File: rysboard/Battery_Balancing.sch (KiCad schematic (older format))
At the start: 50 parts, among them J4 Cell3, J5 Cell2, J6 Cell1, J7 Power_SW

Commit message: NST847BDP6T5G Added, more conections done
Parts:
- removed Q? (x3): PLACEHOLDER, Package_TO_SOT_THT:TO-92_Inline, symbol Transistor_FET:2N7000
- added Q1, Q2: DMP3036SSD-13, Package_SO:SO-8_5.3x6.2mm_P1.27mm, symbol rysboard:DMP3036SSD-13
- U10, U7, U8: renamed from U?; footprint (none) -> Package_SO:SO-8_5.3x6.2mm_P1.27mm
- gave numbers to parts that had none: 40
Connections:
- net PACK-: now also Q1.5 (d), Q1.6 (d)
- net V_BAT_AF_PROT-: now also Q2.1 (S1), Q2.3 (S2)
- net at D12.2 (A2), J6.1 (Pin_1): now also Q2.5 (d), Q2.6 (d), Q2.7 (d), Q2.8 (d)
- net at R15.1: now also Q2.2 (G1), Q2.4 (G2)
- net at R25.1, R30.1, R32.1: now also Q1.7 (d), Q1.8 (d)
- net at D16.1 (K), R33.2, R34.1: now also Q1.4 (G2)
- net at R31.1, R32.2: now also Q1.2 (G1)
- new net: Q1.1 (S1), Q1.3 (S2)
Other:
- moved on the sheet: R15

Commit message: new mosfet footprints
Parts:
- D10, D11, D12: footprint (none) -> Diode_SMD:D_SOD-128
- R15, R16, R17, R18, R19, R20, R21, R22, R23, R24, R30, R37, R38: footprint (none) -> Resistor_SMD:R_0603_1608Metric
- U11: footprint (none) -> Package_SO:TSSOP-24_4.4x7.8mm_P0.65mm
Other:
- note removed: "for lower resistance 2 mosfets on parrarel\n"
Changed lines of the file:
@@
 F 0 "R15" V 1643 3300 50  0000 C CNN
 F 1 "10KR" V 1734 3300 50  0000 C CNN
-F 2 "" V 1780 3300 50  0001 C CNN
+F 2 "Resistor_SMD:R_0603_1608Metric" V 1780 3300 50  0001 C CNN
 F 3 "~" H 1850 3300 50  0001 C CNN
 	1    1850 3300
@@
 F 0 "D10" V 1554 1730 50  0000 L CNN
 F 1 "D_TVS" V 1645 1730 50  0000 L CNN
-F 2 "" H 1600 1650 50  0001 C CNN
+F 2 "Diode_SMD:D_SOD-128" H 1600 1650 50  0001 C CNN
 F 3 "~" H 1600 1650 50  0001 C CNN
 	1    1600 1650
@@
 F 0 "D11" V 1554 2580 50  0000 L CNN
 F 1 "D_TVS" V 1645 2580 50  0000 L CNN
-F 2 "" H 1600 2500 50  0001 C CNN
+F 2 "Diode_SMD:D_SOD-128" H 1600 2500 50  0001 C CNN
 F 3 "~" H 1600 2500 50  0001 C CNN
 	1    1600 2500
@@
 F 0 "D12" V 1554 3380 50  0000 L CNN
 F 1 "D_TVS" V 1645 3380 50  0000 L CNN
-F 2 "" H 1600 3300 50  0001 C CNN
+F 2 "Diode_SMD:D_SOD-128" H 1600 3300 50  0001 C CNN
 F 3 "~" H 1600 3300 50  0001 C CNN
 	1    1600 3300
@@
 	1600 1400 2400 1400
 Connection ~ 1600 1500
-Text Notes 2550 750  0    50   ~ 0
-for lower resistance 2 mosfets on parrarel\n
 Wire Wire Line
 	4350 1350 4750 1350
@@
 F 0 "R24" V 2793 3450 50  0000 C CNN
 F 1 "10KR" V 2884 3450 50  0000 C CNN
-F 2 "" V 2930 3450 50  0001 C CNN
+F 2 "Resistor_SMD:R_0603_1608Metric" V 2930 3450 50  0001 C CNN
 F 3 "~" H 3000 3450 50  0001 C CNN
 	1    3000 3450
@@
 F 0 "R23" V 2793 2300 50  0000 C CNN
 F 1 "10KR" V 2884 2300 50  0000 C CNN
-F 2 "" V 2930 2300 50  0001 C CNN
+F 2 "Resistor_SMD:R_0603_1608Metric" V 2930 2300 50  0001 C CNN
 F 3 "~" H 3000 2300 50  0001 C CNN
 	1    3000 2300
@@
 F 0 "R22" V 2793 1700 50  0000 C CNN
 F 1 "10KR" V 2884 1700 50  0000 C CNN
-F 2 "" V 2930 1700 50  0001 C CNN
+F 2 "Resistor_SMD:R_0603_1608Metric" V 2930 1700 50  0001 C CNN
 F 3 "~" H 3000 1700 50  0001 C CNN
 	1    3000 1700
@@
 F 0 "U11" H 4050 6915 50  0000 C CNN
 F 1 "bq77915" H 4050 6824 50  0000 C CNN
-F 2 "" H 4150 5650 50  0001 C CNN
+F 2 "Package_SO:TSSOP-24_4.4x7.8mm_P0.65mm" H 4150 5650 50  0001 C CNN
 F 3 "" H 4150 5650 50  0001 C CNN
 	1    4050 5750
@@
 F 0 "R38" H 5180 7154 50  0000 R CNN
 F 1 "470KR5%" H 5180 7245 50  0000 R CNN
-F 2 "" V 5180 7200 50  0001 C CNN
+F 2 "Resistor_SMD:R_0603_1608Metric" V 5180 7200 50  0001 C CNN
 F 3 "~" H 5250 7200 50  0001 C CNN
 	1    5250 7200
@@
 F 0 "R17" V 1793 5500 50  0000 C CNN
 F 1 "33R5%" V 1884 5500 50  0000 C CNN
-F 2 "" V 1930 5500 50  0001 C CNN
+F 2 "Resistor_SMD:R_0603_1608Metric" V 1930 5500 50  0001 C CNN
 F 3 "~" H 2000 5500 50  0001 C CNN
 	1    2000 5500
@@
 F 0 "R16" V 1793 4700 50  0000 C CNN
 F 1 "1KR1%" V 1884 4700 50  0000 C CNN
-F 2 "" V 1930 4700 50  0001 C CNN
+F 2 "Resistor_SMD:R_0603_1608Metric" V 1930 4700 50  0001 C CNN
 F 3 "~" H 2000 4700 50  0001 C CNN
 	1    2000 4700
@@
 F 0 "R37" V 4900 6100 50  0000 C CNN
 F 1 "470KR1%" V 5000 6100 50  0000 C CNN
-F 2 "" V 5030 6100 50  0001 C CNN
+F 2 "Resistor_SMD:R_0603_1608Metric" V 5030 6100 50  0001 C CNN
 F 3 "~" H 5100 6100 50  0001 C CNN
 	1    5100 6100
@@
 F 0 "R21" H 2850 6900 50  0000 R CNN
 F 1 "100R" H 3000 7150 50  0000 R CNN
-F 2 "" V 2830 6950 50  0001 C CNN
+F 2 "Resistor_SMD:R_0603_1608Metric" V 2830 6950 50  0001 C CNN
 F 3 "~" H 2900 6950 50  0001 C CNN
 	1    2900 6950
@@
 F 0 "R30" H 3350 6900 50  0000 R CNN
 F 1 "100R" H 3300 7100 50  0000 R CNN
-F 2 "" V 3130 6950 50  0001 C CNN
+F 2 "Resistor_SMD:R_0603_1608Metric" V 3130 6950 50  0001 C CNN
 F 3 "~" H 3200 6950 50  0001 C CNN
 	1    3200 6950
@@
 F 0 "R18" V 1793 6000 50  0000 C CNN
 F 1 "33R5%" V 1884 6000 50  0000 C CNN
-F 2 "" V 1930 6000 50  0001 C CNN
+F 2 "Resistor_SMD:R_0603_1608Metric" V 1930 6000 50  0001 C CNN
 F 3 "~" H 2000 6000 50  0001 C CNN
 	1    2000 6000
@@
 F 0 "R19" V 1793 6500 50  0000 C CNN
 F 1 "33R5%" V 1884 6500 50  0000 C CNN
-F 2 "" V 1930 6500 50  0001 C CNN
+F 2 "Resistor_SMD:R_0603_1608Metric" V 1930 6500 50  0001 C CNN
 F 3 "~" H 2000 6500 50  0001 C CNN
 	1    2000 6500
@@
 F 0 "R20" V 1793 7100 50  0000 C CNN
 F 1 "33R5%" V 1884 7100 50  0000 C CNN
-F 2 "" V 1930 7100 50  0001 C CNN
+F 2 "Resistor_SMD:R_0603_1608Metric" V 1930 7100 50  0001 C CNN
 F 3 "~" H 2000 7100 50  0001 C CNN
 	1    2000 7100

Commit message: Fixed library, added a few MOSFET layouts
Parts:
- removed D14, D15: D_Zener, symbol Device:D_Zener
- removed Q2: DMP3036SSD-13, Package_SO:SO-8_5.3x6.2mm_P1.27mm, symbol rysboard:DMP3036SSD-13
- removed U10, U7, U8: DMP3036SSD, Package_SO:SO-8_5.3x6.2mm_P1.27mm, symbol rysboard:DMP3036SSD
- added Q13: SI7997DP-T1-GE3, Package_SO:PowerPAK_SO-8_Dual, symbol rysboard:SI7997DP-T1-GE3
- added Q14: DMP2075UFDB-7-alt, SamacSys_Parts:DMP2075UFDB7, symbol SamacSys_Parts:DMP2075UFDB-7-alt
- added Q?: Si7938DP-T1-GE3, Package_SO:PowerPAK_SO-8_Dual, symbol rysboard:Si7938DP-T1-GE3
- Q1: footprint Package_SO:SO-8_5.3x6.2mm_P1.27mm -> Package_SO:SO-8_3.9x4.9mm_P1.27mm
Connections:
- net V_BAT_AF_PROT-: now also Q?.1 (S1)
- net V_CELL_1: now also Q14.1 (S1)
- net V_CELL_2: now also Q14.4 (S2)
- net V_CELL_3: now also Q13.6 (D1)
- net at D10.2 (A2), D11.1 (A1), J5.2 (Pin_2): now also J6.1 (Pin_1), Q14.3 (D2_1), Q14.8 (D2_2); no longer J4.1 (Pin_1)
- net at J4.2 (Pin_2): now also D11.2 (A2), D12.1 (A1), J5.1 (Pin_1), R15.2, Q14.6 (D1_1), Q14.7 (D1_2); no longer D10.1 (A1)
- net at D12.2 (A2): now also J4.1 (Pin_1), Q?.5 (D1); no longer J6.1 (Pin_1)
- net at R24.2: now also Q14.2 (G1)
- net at R23.2: now also Q14.5 (G2)
- net at R15.1: now also Q?.2 (G1)
- net at D13.1 (K): now also Q13.1 (S1), Q13.3 (S2)
- net at D13.2 (A), R22.2: now also Q13.2 (G1), Q13.4 (G2)
- new net: D10.1 (A1), J6.2 (Pin_2), Q13.5 (D1)
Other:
- moved on the sheet: J4, J6, R15

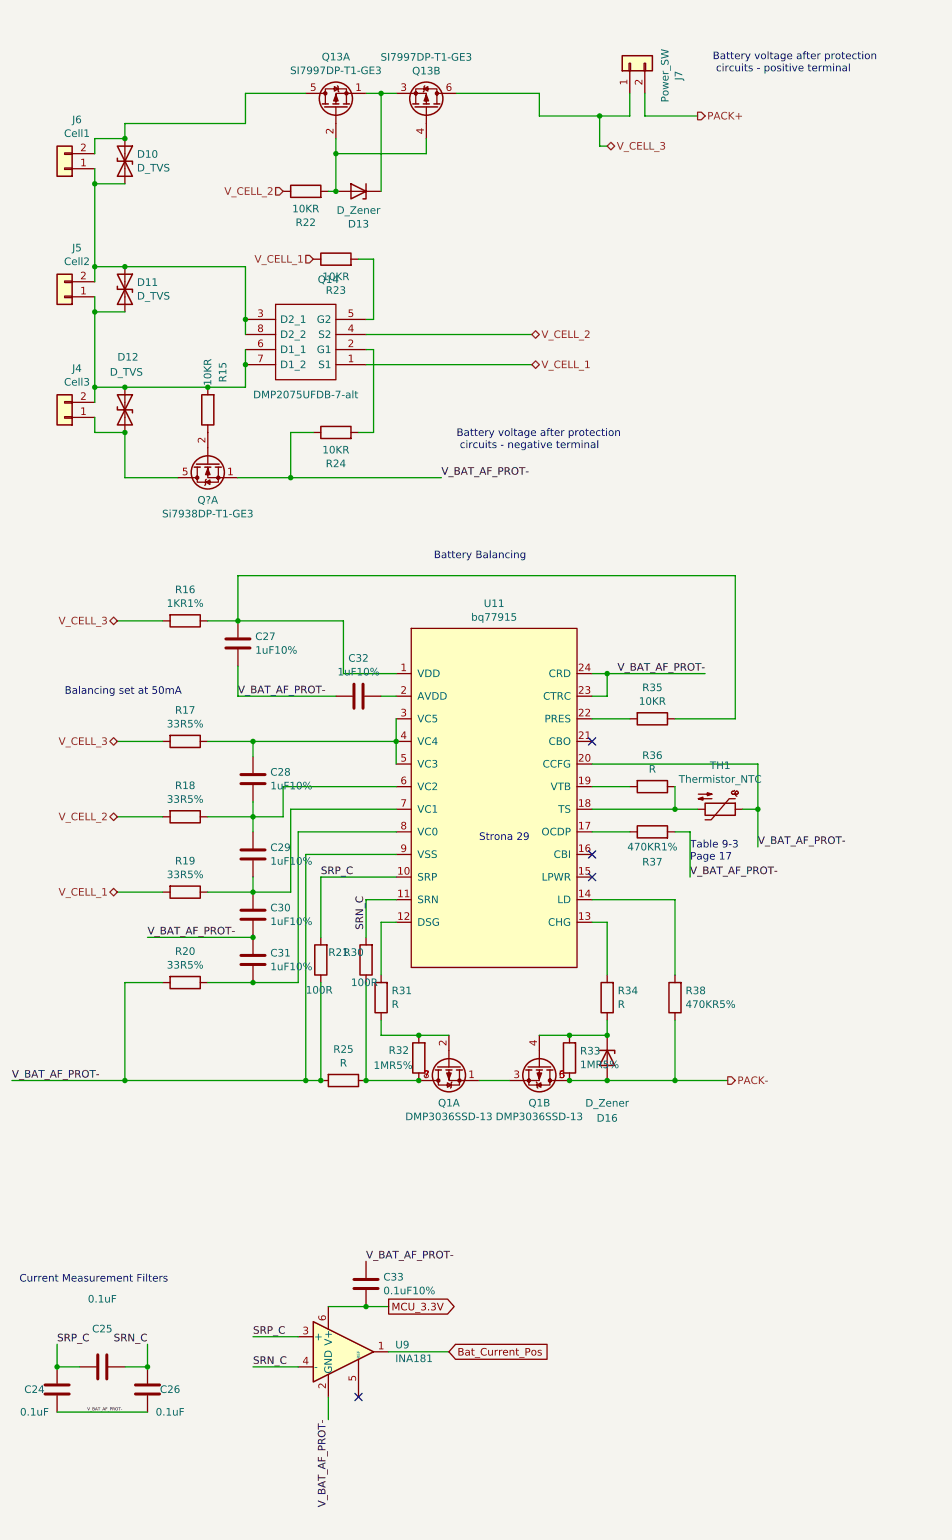
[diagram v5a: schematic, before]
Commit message: battery Balancing specified
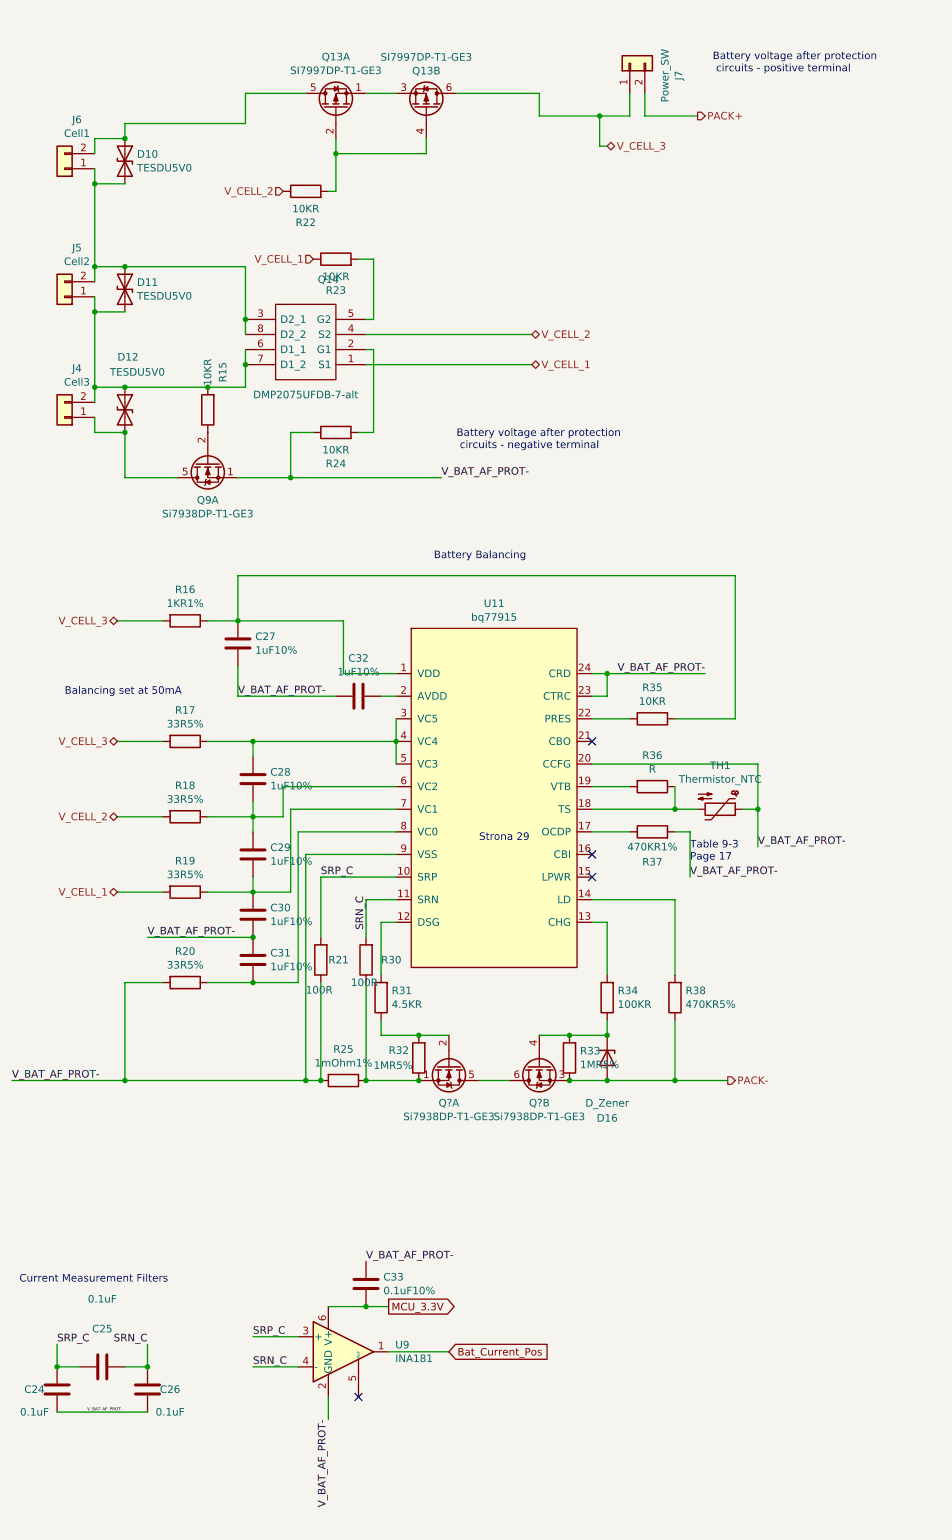
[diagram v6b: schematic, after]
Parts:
- removed D13: D_Zener, symbol Device:D_Zener
- removed Q1: DMP3036SSD-13, Package_SO:SO-8_3.9x4.9mm_P1.27mm, symbol rysboard:DMP3036SSD-13
- added Q? (x2): Si7938DP-T1-GE3, Package_SO:PowerPAK_SO-8_Dual, symbol rysboard:Si7938DP-T1-GE3
- C24, C25, C26, C33: footprint (none) -> Capacitor_SMD:C_0603_1608Metric_Pad1.05x0.95mm_HandSolder
- D10, D11, D12: value D_TVS -> TESDU5V0; footprint Diode_SMD:D_SOD-128 -> Diode_SMD:D_0603_1608Metric_Pad1.05x0.95mm_HandSolder
- R25: value R -> 1mOhm1%; footprint (none) -> Resistor_SMD:R_1206_3216Metric_Pad1.42x1.75mm_HandSolder
- R31: value R -> 4.5KR; footprint (none) -> Resistor_SMD:R_0603_1608Metric_Pad1.05x0.95mm_HandSolder
- R34: value R -> 100KR; footprint (none) -> Resistor_SMD:R_0603_1608Metric_Pad1.05x0.95mm_HandSolder
- gave numbers to parts that had none: 1
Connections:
- net PACK-: now also Q?.3 (S2)
- net at R25.1, R30.1, R32.1: now also Q?.1 (S1)
- net at D16.1 (K), R33.2, R34.1: now also Q?.4 (G2)
- net at R31.1, R32.2: now also Q?.2 (G1)
- new net: Q?.5 (D1), Q?.6 (D1)
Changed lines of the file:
@@
 P 1600 1650
 F 0 "D10" V 1554 1730 50  0000 L CNN
-F 1 "D_TVS" V 1645 1730 50  0000 L CNN
-F 2 "Diode_SMD:D_SOD-128" H 1600 1650 50  0001 C CNN
+F 1 "TESDU5V0 " V 1645 1730 50  0000 L CNN
+F 2 "Diode_SMD:D_0603_1608Metric_Pad1.05x0.95mm_HandSolder" H 1600 1650 50  0001 C CNN
 F 3 "~" H 1600 1650 50  0001 C CNN
 	1    1600 1650
@@
 P 1600 2500
 F 0 "D11" V 1554 2580 50  0000 L CNN
-F 1 "D_TVS" V 1645 2580 50  0000 L CNN
-F 2 "Diode_SMD:D_SOD-128" H 1600 2500 50  0001 C CNN
+F 1 "TESDU5V0 " V 1645 2580 50  0000 L CNN
+F 2 "Diode_SMD:D_0603_1608Metric_Pad1.05x0.95mm_HandSolder" H 1600 2500 50  0001 C CNN
 F 3 "~" H 1600 2500 50  0001 C CNN
 	1    1600 2500
@@
 P 1600 3300
 F 0 "D12" V 1250 3250 50  0000 L CNN
-F 1 "D_TVS" V 1350 3200 50  0000 L CNN
-F 2 "Diode_SMD:D_SOD-128" H 1600 3300 50  0001 C CNN
+F 1 "TESDU5V0 " V 1350 3200 50  0000 L CNN
+F 2 "Diode_SMD:D_0603_1608Metric_Pad1.05x0.95mm_HandSolder" H 1600 3300 50  0001 C CNN
 F 3 "~" H 1600 3300 50  0001 C CNN
 	1    1600 3300
@@
 P 3050 7750
 F 0 "R25" V 2843 7750 50  0000 C CNN
-F 1 "R" V 2934 7750 50  0000 C CNN
-F 2 "" V 2980 7750 50  0001 C CNN
+F 1 "1mOhm1%" V 2934 7750 50  0000 C CNN
+F 2 "Resistor_SMD:R_1206_3216Metric_Pad1.42x1.75mm_HandSolder" V 2980 7750 50  0001 C CNN
 F 3 "~" H 3050 7750 50  0001 C CNN
 	1    3050 7750
@@
 P 3300 7200
 F 0 "R31" H 3230 7154 50  0000 R CNN
-F 1 "R" H 3230 7245 50  0000 R CNN
-F 2 "" V 3230 7200 50  0001 C CNN
+F 1 "4.5KR" H 3230 7245 50  0000 R CNN
+F 2 "Resistor_SMD:R_0603_1608Metric_Pad1.05x0.95mm_HandSolder" V 3230 7200 50  0001 C CNN
 F 3 "~" H 3300 7200 50  0001 C CNN
 	1    3300 7200
@@
 P 4800 7200
 F 0 "R34" H 4730 7154 50  0000 R CNN
-F 1 "R" H 4730 7245 50  0000 R CNN
-F 2 "" V 4730 7200 50  0001 C CNN
+F 1 "100KR" H 4730 7245 50  0000 R CNN
+F 2 "Resistor_SMD:R_0603_1608Metric_Pad1.05x0.95mm_HandSolder" V 4730 7200 50  0001 C CNN
 F 3 "~" H 4800 7200 50  0001 C CNN
 	1    4800 7200
@@
 U 1 1 5FFCDDDB
 P 2900 6950
-F 0 "R21" H 2850 6900 50  0000 R CNN
+F 0 "R21" H 2850 6950 50  0000 R CNN
 F 1 "100R" H 3000 7150 50  0000 R CNN
 F 2 "Resistor_SMD:R_0603_1608Metric" V 2830 6950 50  0001 C CNN
@@
 U 1 1 5FFCE02A
 P 3200 6950
-F 0 "R30" H 3350 6900 50  0000 R CNN
+F 0 "R30" H 3100 6950 50  0000 R CNN
 F 1 "100R" H 3300 7100 50  0000 R CNN
 F 2 "Resistor_SMD:R_0603_1608Metric" V 3130 6950 50  0001 C CNN
@@
 F 0 "C25" V 1702 9650 50  0000 C CNN
 F 1 "0.1uF" V 1900 9650 50  0000 C CNN
-F 2 "" H 1488 9500 50  0001 C CNN
+F 2 "Capacitor_SMD:C_0603_1608Metric_Pad1.05x0.95mm_HandSolder" H 1488 9500 50  0001 C CNN
 F 3 "~" H 1450 9650 50  0001 C CNN
 	1    1450 9650
@@
 F 0 "C24" H 1000 9800 50  0000 C CNN
 F 1 "0.1uF" H 1000 9650 50  0000 C CNN
-F 2 "" H 1188 9650 50  0001 C CNN
+F 2 "Capacitor_SMD:C_0603_1608Metric_Pad1.05x0.95mm_HandSolder" H 1188 9650 50  0001 C CNN
 F 3 "~" H 1150 9800 50  0001 C CNN
 	1    1150 9800
@@
 F 0 "C26" H 1900 9800 50  0000 C CNN
 F 1 "0.1uF" H 1900 9650 50  0000 C CNN
-F 2 "" H 1788 9650 50  0001 C CNN
+F 2 "Capacitor_SMD:C_0603_1608Metric_Pad1.05x0.95mm_HandSolder" H 1788 9650 50  0001 C CNN
 F 3 "~" H 1750 9800 50  0001 C CNN
 	1    1750 9800
@@
 F 0 "C33" H 3085 9054 50  0000 R CNN
 F 1 "0.1uF10%" H 3085 9145 50  0000 R CNN
-F 2 "" H 3238 8950 50  0001 C CNN
+F 2 "Capacitor_SMD:C_0603_1608Metric_Pad1.05x0.95mm_HandSolder" H 3238 8950 50  0001 C CNN
 F 3 "~" H 3200 9100 50  0001 C CNN
 	1    3200 9100
@@
 	0    -1   -1   0
 $EndComp
-$Comp
-L Device:D_Zener D13
-U 1 1 6044AEC7
-P 3150 1850
-F 0 "D13" H 3150 2067 50  0000 C CNN
-F 1 "D_Zener" H 3150 1976 50  0000 C CNN
-F 2 "" H 3150 1850 50  0001 C CNN
-F 3 "~" H 3150 1850 50  0001 C CNN
-	1    3150 1850
-	-1   0    0    1
-$EndComp
-Wire Wire Line
-	3200 1200 3300 1200
-Wire Wire Line
-	3300 1200 3300 1850
-Connection ~ 3300 1200
-Wire Wire Line
-	3300 1200 3400 1200
 Wire Wire Line
 	3000 1850 3000 1600
@@
 Wire Wire Line
 	2950 1850 3000 1850
-Connection ~ 3000 1850
 Text HLabel 2650 1850 0    50   Input ~ 0
 V_CELL_2
@@
 	1600 3150 2150 3150
 $Comp
-L rysboard:Si7938DP-T1-GE3 Q?
+L rysboard:Si7938DP-T1-GE3 Q9
 U 1 1 605A83B7
 P 2150 3650
-F 0 "Q?" V 2399 3650 50  0000 C CNN
+F 0 "Q9" V 2399 3650 50  0000 C CNN
 F 1 "Si7938DP-T1-GE3" V 2490 3650 50  0000 C CNN
 F 2 "Package_SO:PowerPAK_SO-8_Dual" H 2350 3575 50  0001 L CIN
@@
 	0    -1   1    0
 $EndComp
-Connection ~ 4550 7750
-$Comp
-L rysboard:DMP3036SSD-13 Q1
-U 2 1 6052B6DB
+$Comp
+L rysboard:Si7938DP-T1-GE3 Q?
+U 1 1 605FA748
+P 3750 7650
+F 0 "Q?" V 3999 7650 50  0000 C CNN
+F 1 "Si7938DP-T1-GE3" V 4090 7650 50  0000 C CNN
+F 2 "Package_SO:PowerPAK_SO-8_Dual" H 3950 7575 50  0001 L CIN
+F 3 "" H 3750 7650 50  0001 L CNN
+	1    3750 7650
+	0    1    1    0
+$EndComp
+Connection ~ 3550 7750
+$Comp
+L rysboard:Si7938DP-T1-GE3 Q?
+U 2 1 605FB9FA
 P 4350 7650
-F 0 "Q1" V 4599 7650 50  0000 C CNN
-F 1 "DMP3036SSD-13" V 4690 7650 50  0000 C CNN
-F 2 "Package_SO:SO-8_3.9x4.9mm_P1.27mm" H 4550 7575 50  0001 L CIN
+F 0 "Q?" V 4599 7650 50  0000 C CNN
+F 1 "Si7938DP-T1-GE3" V 4690 7650 50  0000 C CNN
+F 2 "Package_SO:PowerPAK_SO-8_Dual" H 4550 7575 50  0001 L CIN
 F 3 "" H 4350 7650 50  0001 L CNN
 	2    4350 7650
-	0    1    1    0
-$EndComp
-Connection ~ 3550 7750
-$Comp
-L rysboard:DMP3036SSD-13 Q1
-U 1 1 6052EF35
-P 3750 7650
-F 0 "Q1" V 3999 7650 50  0000 C CNN
-F 1 "DMP3036SSD-13" V 4090 7650 50  0000 C CNN
-F 2 "Package_SO:SO-8_3.9x4.9mm_P1.27mm" H 3950 7575 50  0001 L CIN
-F 3 "" H 3750 7650 50  0001 L CNN
-	1    3750 7650
 	0    -1   1    0
 $EndComp
+Connection ~ 4550 7750
+Wire Wire Line
+	3200 1200 3400 1200
 $EndSCHEMATC

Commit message: more work done
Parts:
- gave numbers to parts that had none: 1
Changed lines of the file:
@@
 $EndComp
 $Comp
-L rysboard:Si7938DP-T1-GE3 Q?
+L rysboard:Si7938DP-T1-GE3 Q12
 U 1 1 605FA748
 P 3750 7650
-F 0 "Q?" V 3999 7650 50  0000 C CNN
+F 0 "Q12" V 3999 7650 50  0000 C CNN
 F 1 "Si7938DP-T1-GE3" V 4090 7650 50  0000 C CNN
 F 2 "Package_SO:PowerPAK_SO-8_Dual" H 3950 7575 50  0001 L CIN
@@
 Connection ~ 3550 7750
 $Comp
-L rysboard:Si7938DP-T1-GE3 Q?
+L rysboard:Si7938DP-T1-GE3 Q12
 U 2 1 605FB9FA
 P 4350 7650
-F 0 "Q?" V 4599 7650 50  0000 C CNN
+F 0 "Q12" V 4599 7650 50  0000 C CNN
 F 1 "Si7938DP-T1-GE3" V 4690 7650 50  0000 C CNN
 F 2 "Package_SO:PowerPAK_SO-8_Dual" H 4550 7575 50  0001 L CIN

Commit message: more footprints
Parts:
- C24, C25, C26: footprint Capacitor_SMD:C_0603_1608Metric_Pad1.05x0.95mm_HandSolder -> Capacitor_SMD:C_0603_1608Metric
- C27, C28, C29, C30, C31, C32: footprint (none) -> Capacitor_SMD:C_0603_1608Metric
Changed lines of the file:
@@
 F 0 "C25" V 1702 9650 50  0000 C CNN
 F 1 "0.1uF" V 1900 9650 50  0000 C CNN
-F 2 "Capacitor_SMD:C_0603_1608Metric_Pad1.05x0.95mm_HandSolder" H 1488 9500 50  0001 C CNN
+F 2 "Capacitor_SMD:C_0603_1608Metric" H 1488 9500 50  0001 C CNN
 F 3 "~" H 1450 9650 50  0001 C CNN
 	1    1450 9650
@@
 F 0 "C24" H 1000 9800 50  0000 C CNN
 F 1 "0.1uF" H 1000 9650 50  0000 C CNN
-F 2 "Capacitor_SMD:C_0603_1608Metric_Pad1.05x0.95mm_HandSolder" H 1188 9650 50  0001 C CNN
+F 2 "Capacitor_SMD:C_0603_1608Metric" H 1188 9650 50  0001 C CNN
 F 3 "~" H 1150 9800 50  0001 C CNN
 	1    1150 9800
@@
 F 0 "C26" H 1900 9800 50  0000 C CNN
 F 1 "0.1uF" H 1900 9650 50  0000 C CNN
-F 2 "Capacitor_SMD:C_0603_1608Metric_Pad1.05x0.95mm_HandSolder" H 1788 9650 50  0001 C CNN
+F 2 "Capacitor_SMD:C_0603_1608Metric" H 1788 9650 50  0001 C CNN
 F 3 "~" H 1750 9800 50  0001 C CNN
 	1    1750 9800
@@
 F 0 "C27" H 2235 4804 50  0000 R CNN
 F 1 "1uF10%" H 2235 4895 50  0000 R CNN
-F 2 "" H 2388 4700 50  0001 C CNN
+F 2 "Capacitor_SMD:C_0603_1608Metric" H 2388 4700 50  0001 C CNN
 F 3 "~" H 2350 4850 50  0001 C CNN
 	1    2350 4850
@@
 F 0 "C28" H 2335 5704 50  0000 R CNN
 F 1 "1uF10%" H 2335 5795 50  0000 R CNN
-F 2 "" H 2488 5600 50  0001 C CNN
+F 2 "Capacitor_SMD:C_0603_1608Metric" H 2488 5600 50  0001 C CNN
 F 3 "~" H 2450 5750 50  0001 C CNN
 	1    2450 5750
@@
 F 0 "C29" H 2335 6204 50  0000 R CNN
 F 1 "1uF10%" H 2335 6295 50  0000 R CNN
-F 2 "" H 2488 6100 50  0001 C CNN
+F 2 "Capacitor_SMD:C_0603_1608Metric" H 2488 6100 50  0001 C CNN
 F 3 "~" H 2450 6250 50  0001 C CNN
 	1    2450 6250
@@
 F 0 "C30" H 2335 6604 50  0000 R CNN
 F 1 "1uF10%" H 2335 6695 50  0000 R CNN
-F 2 "" H 2488 6500 50  0001 C CNN
+F 2 "Capacitor_SMD:C_0603_1608Metric" H 2488 6500 50  0001 C CNN
 F 3 "~" H 2450 6650 50  0001 C CNN
 	1    2450 6650
@@
 F 0 "C31" H 2335 6904 50  0000 R CNN
 F 1 "1uF10%" H 2335 6995 50  0000 R CNN
-F 2 "" H 2488 6800 50  0001 C CNN
+F 2 "Capacitor_SMD:C_0603_1608Metric" H 2488 6800 50  0001 C CNN
 F 3 "~" H 2450 6950 50  0001 C CNN
 	1    2450 6950
@@
 F 0 "C32" V 3402 5200 50  0000 C CNN
 F 1 "1uF10%" V 3311 5200 50  0000 C CNN
-F 2 "" H 3188 5050 50  0001 C CNN
+F 2 "Capacitor_SMD:C_0603_1608Metric" H 3188 5050 50  0001 C CNN
 F 3 "~" H 3150 5200 50  0001 C CNN
 	1    3150 5200
